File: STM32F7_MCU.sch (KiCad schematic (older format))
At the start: 49 parts, among them IC4 STM32F769IIT6, IC5 LD1117ADT33TR, Y1 25MHz, Y2 XTAL016178-85SMX

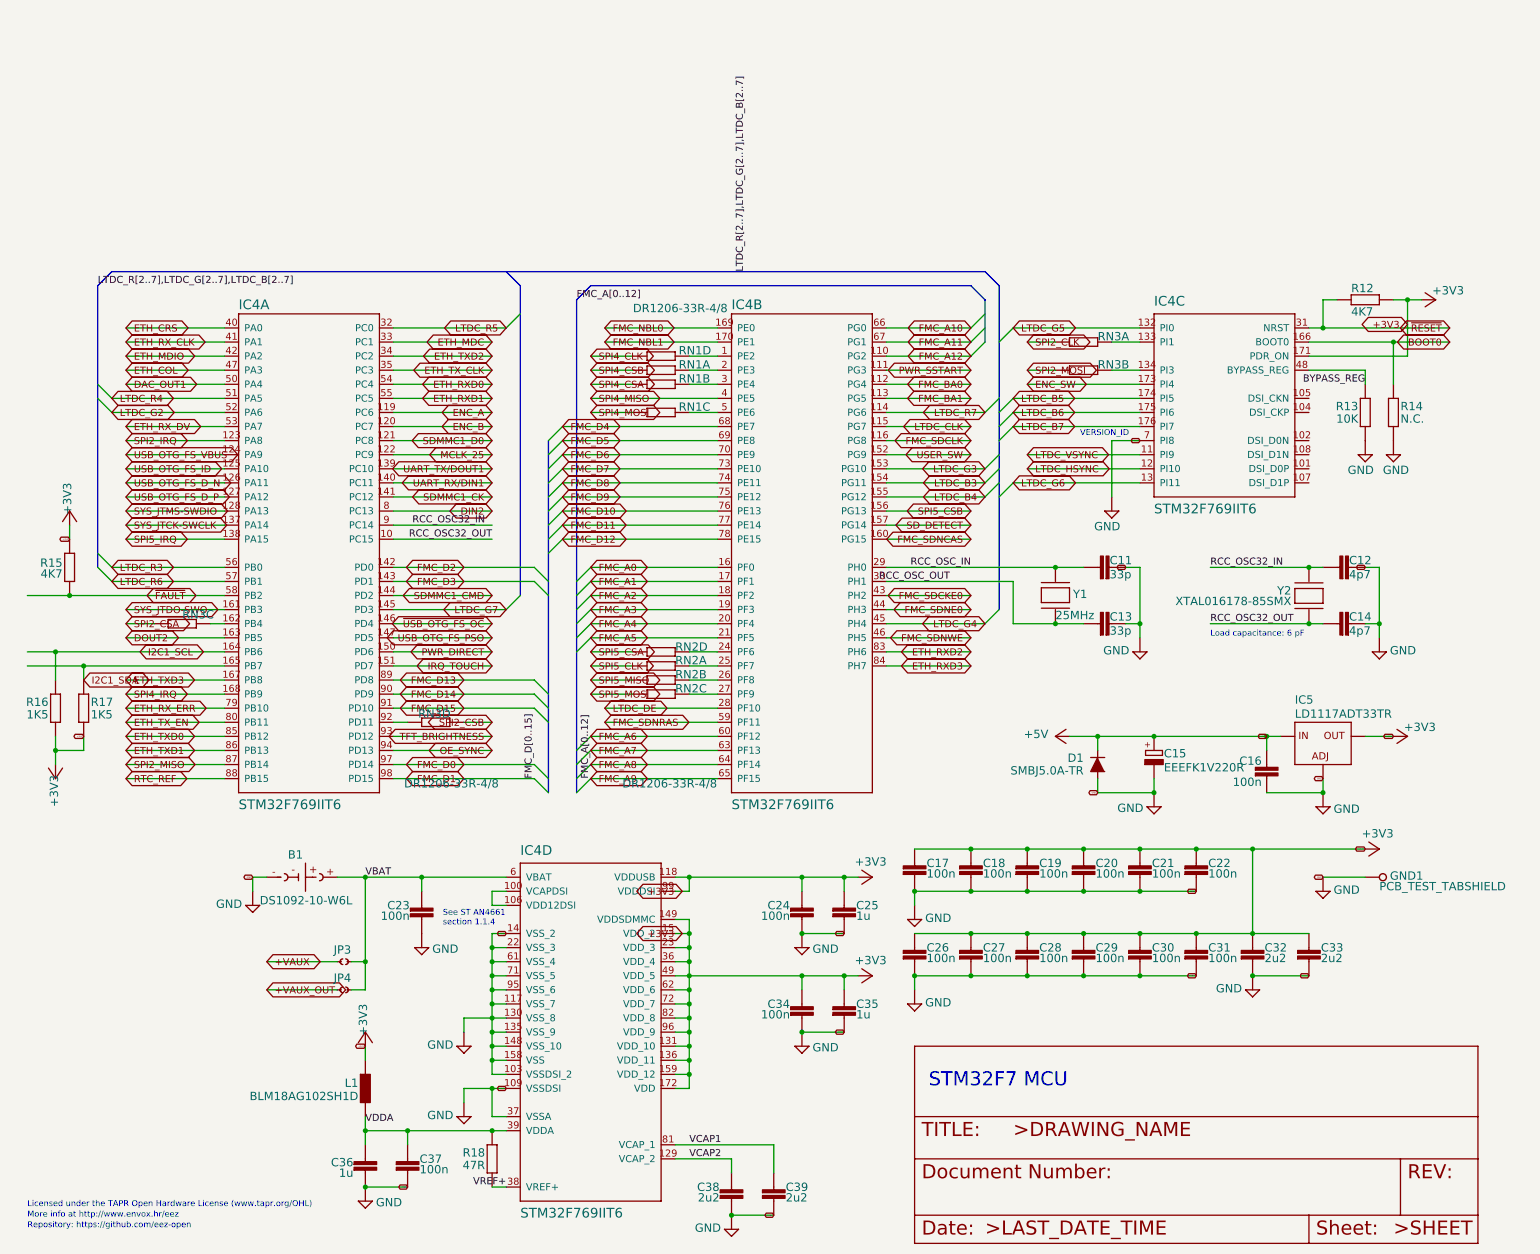
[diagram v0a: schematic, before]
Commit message: Assigning parts - netlitst to pcb
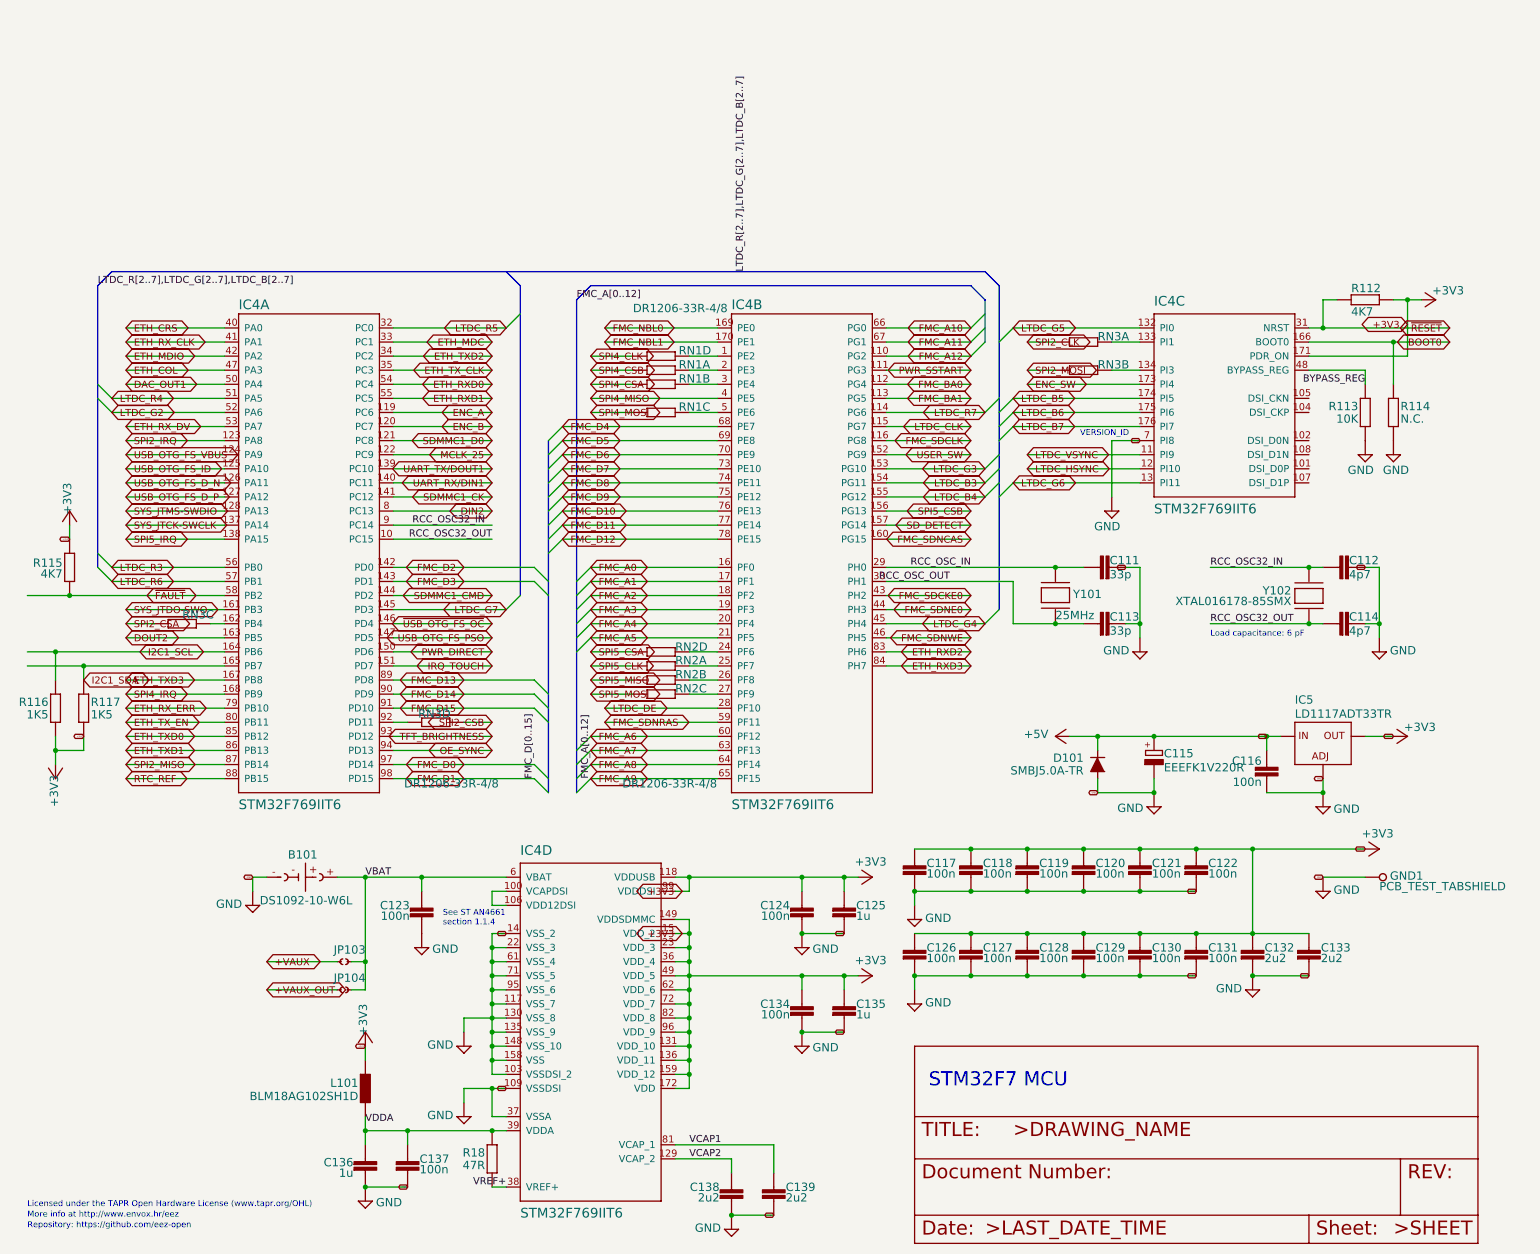
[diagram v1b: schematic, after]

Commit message: New annotation - All STM32 parts are +100
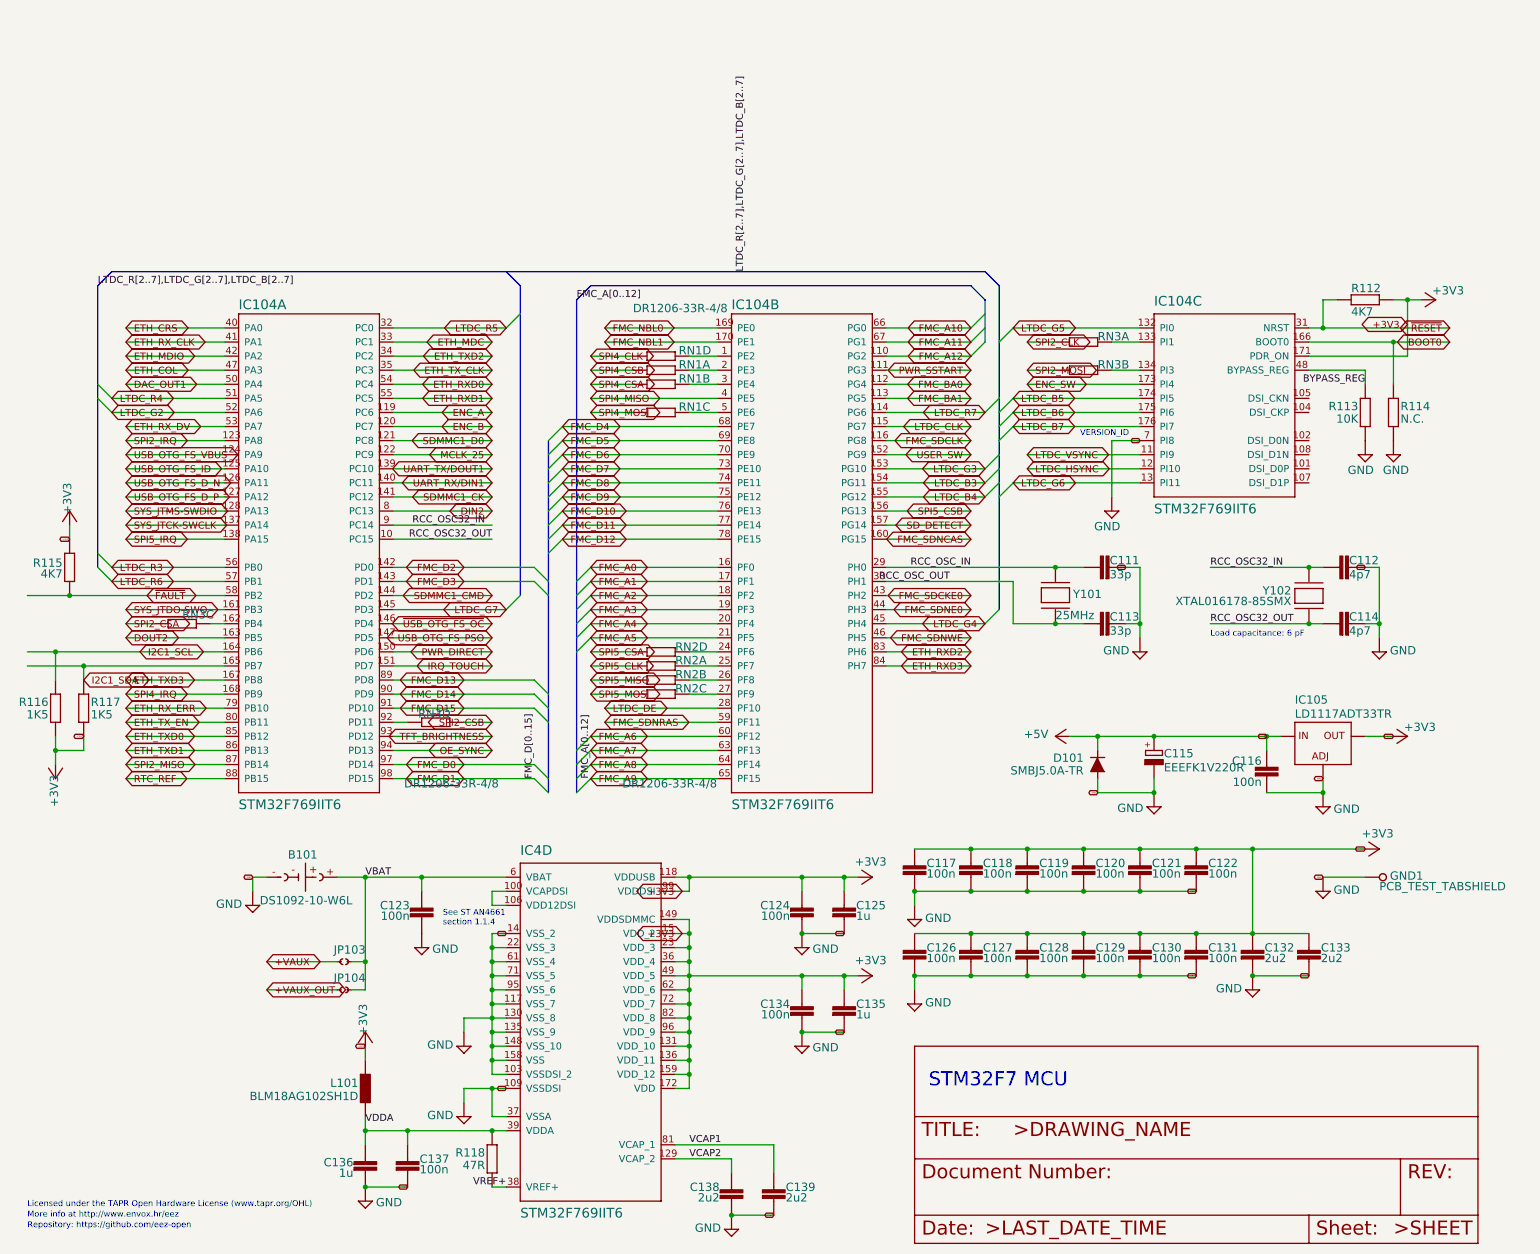
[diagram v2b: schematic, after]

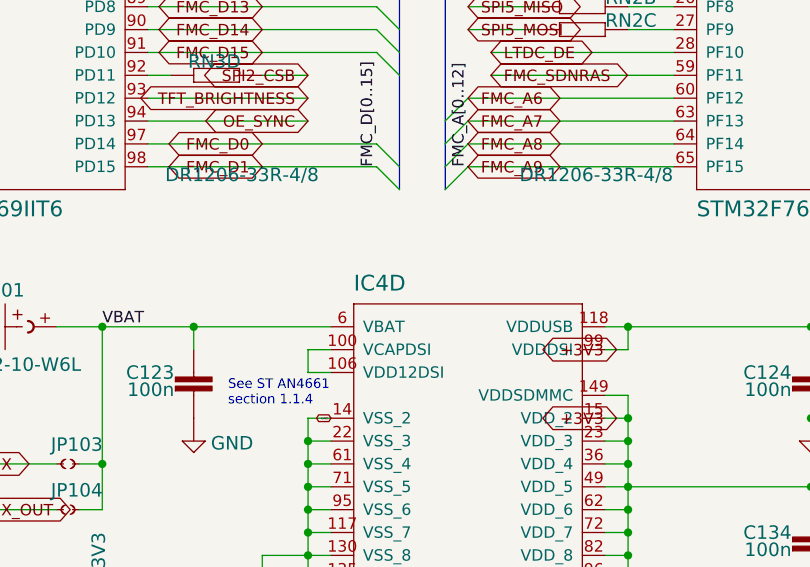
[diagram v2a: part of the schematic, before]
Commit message: All STM32 parts are now +100, moving parts to original position
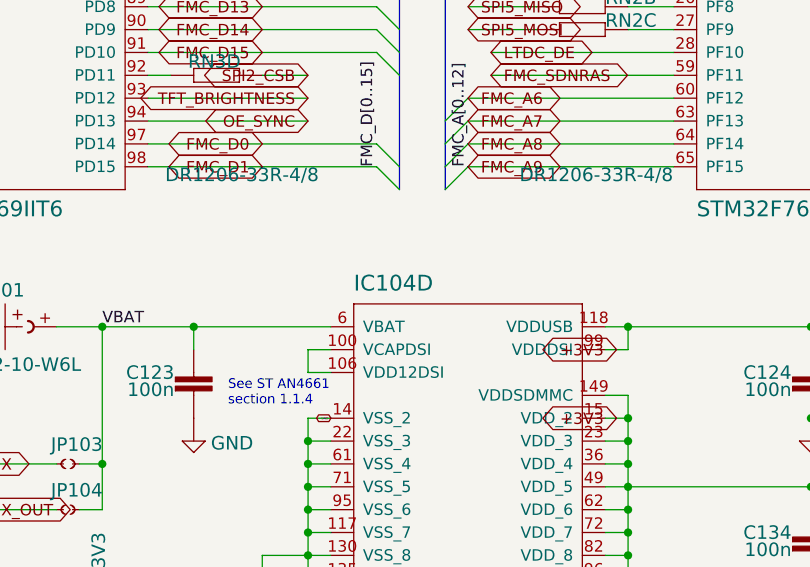
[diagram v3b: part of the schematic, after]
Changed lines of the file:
@@
 AR Path="/5F88D05D/E4FF245AB1CDB4E3" Ref="IC4"  Part="4"
 AR Path="/5F88BD9A/E4FF245AB1CDB4E3" Ref="IC4"  Part="4"
-AR Path="/5F88BD9A/B1CDB4E3" Ref="IC4"  Part="4"
-F 0 "IC4" H 4500 6450 69  0000 L BNN
+AR Path="/5F88BD9A/B1CDB4E3" Ref="IC104"  Part="4"
+F 0 "IC104" H 4500 6450 69  0000 L BNN
 F 1 "STM32F769IIT6" H 4500 3875 69  0000 L BNN
 F 2 "EEZ DIB MCU r3B4:LQFP-176_24X24MM" H 4500 6400 50  0001 C CNN

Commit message: Adding default parts
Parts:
- C11, C12, C13, C14, C16, C17, C18, C19, C20, C21, C22, C23, C24, C26, C27, C28, C29, C30, C31, C34, C37: footprint EEZ DIB MCU r3B4:C0603 -> Capacitor_SMD:C_0603_1608Metric
- C25, C32, C33, C35, C36, C38, C39: footprint EEZ DIB MCU r3B4:C0805 -> Capacitor_SMD:C_0805_2012Metric
- IC4: footprint EEZ DIB MCU r3B4:LQFP-176_24X24MM -> Package_QFP:LQFP-176_24x24mm_P0.5mm
- R12, R13, R14, R15, R16, R17, R18: footprint EEZ DIB MCU r3B4:R0805 -> Resistor_SMD:R_0805_2012Metric
